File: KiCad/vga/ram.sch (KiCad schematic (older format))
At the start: 4 parts, among them U2 61256-15, U3 61256-15, U4 61256-15, U5 61256-15

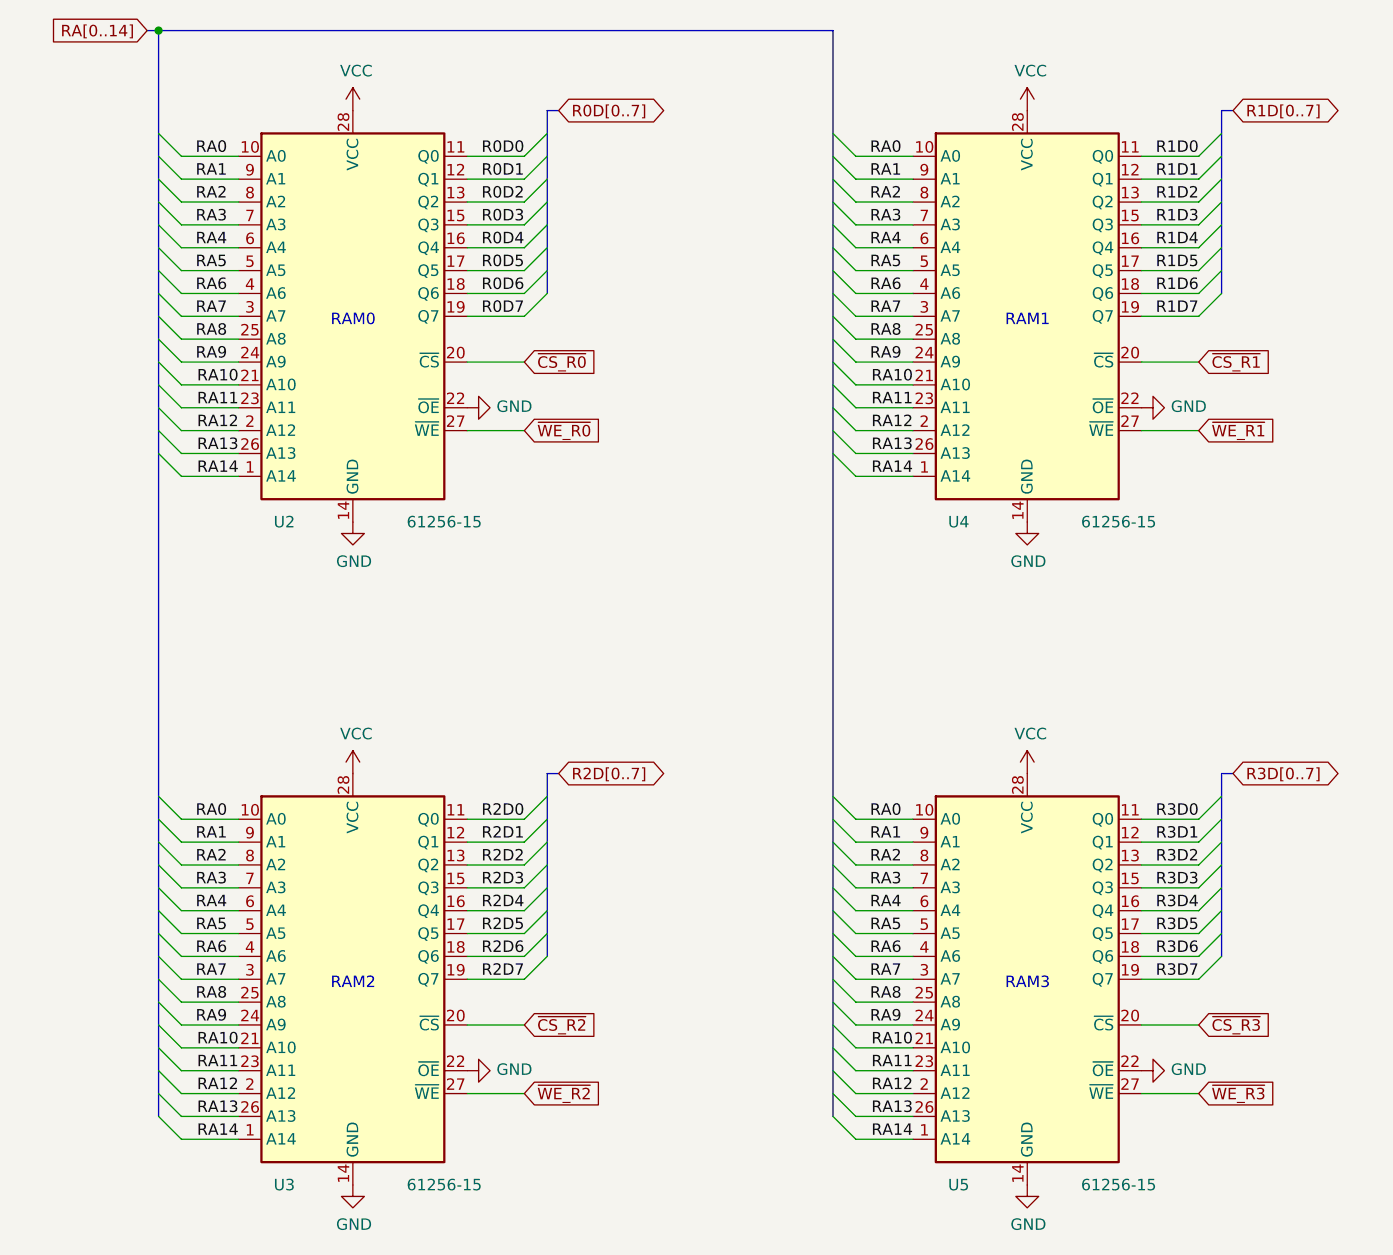
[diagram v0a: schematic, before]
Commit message: Updated graphics adapter
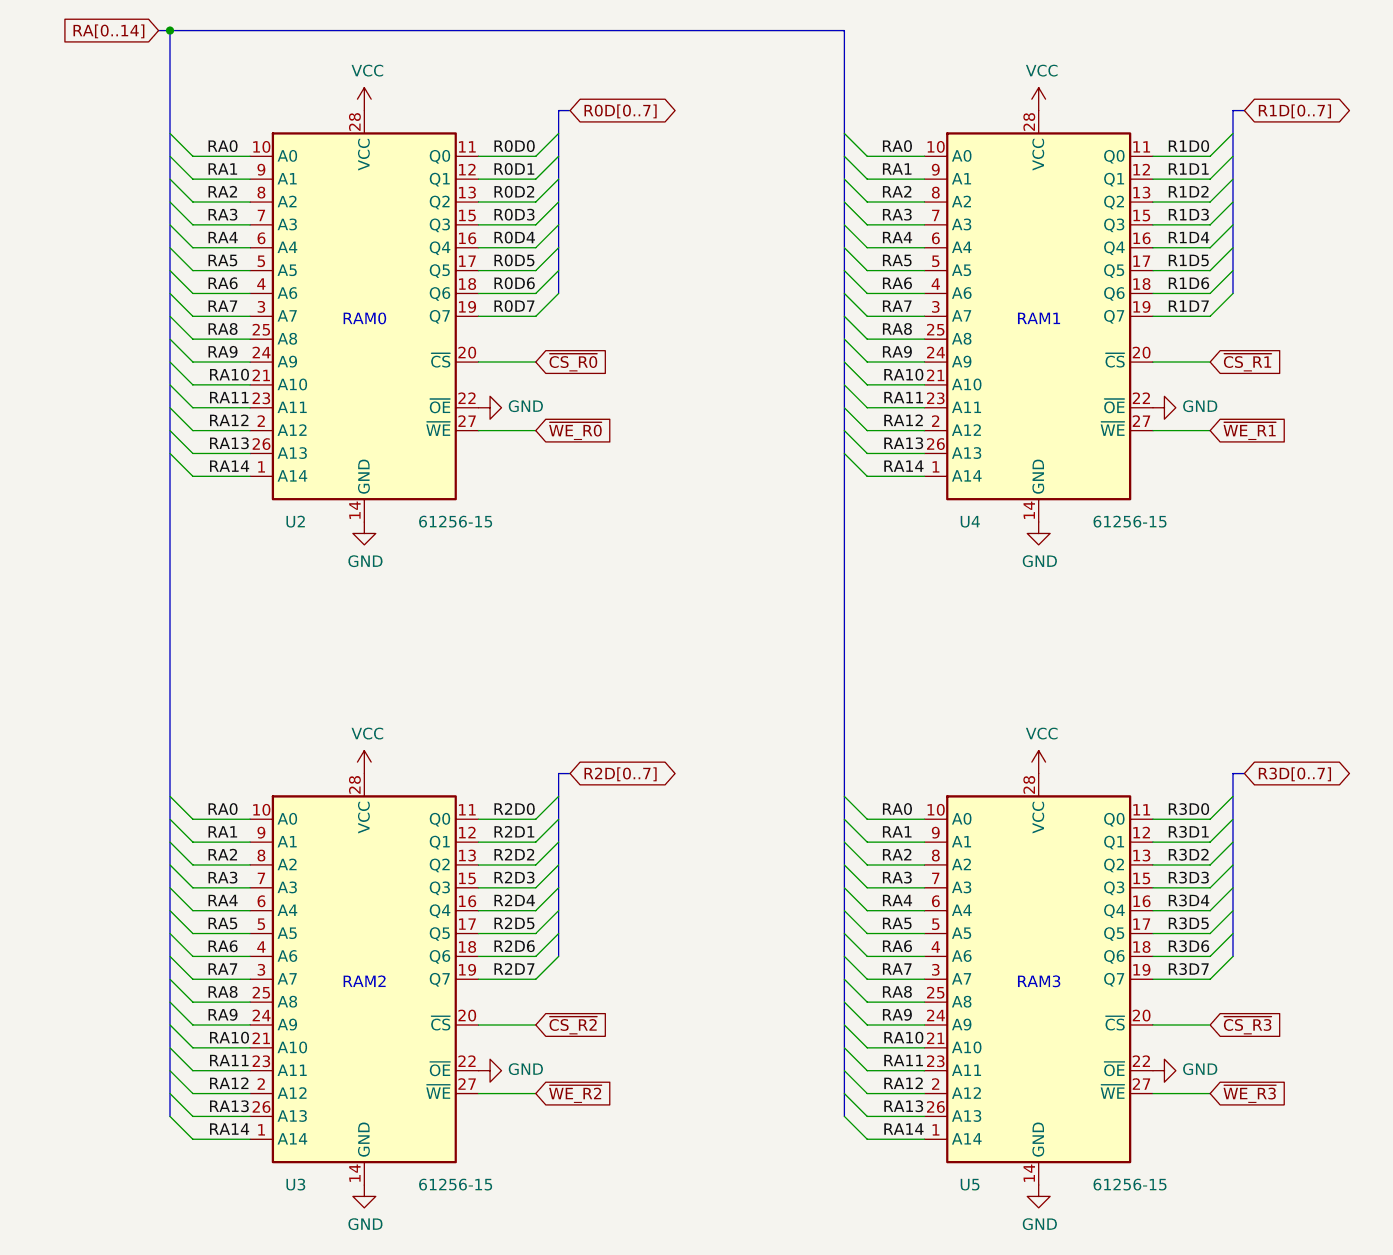
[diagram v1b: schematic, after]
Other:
- moved on the sheet: U2, U3, U4, U5

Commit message: Replaced MAX7000 CPLD with MAX II in graphics adapter. PCB redesign with smaller size.
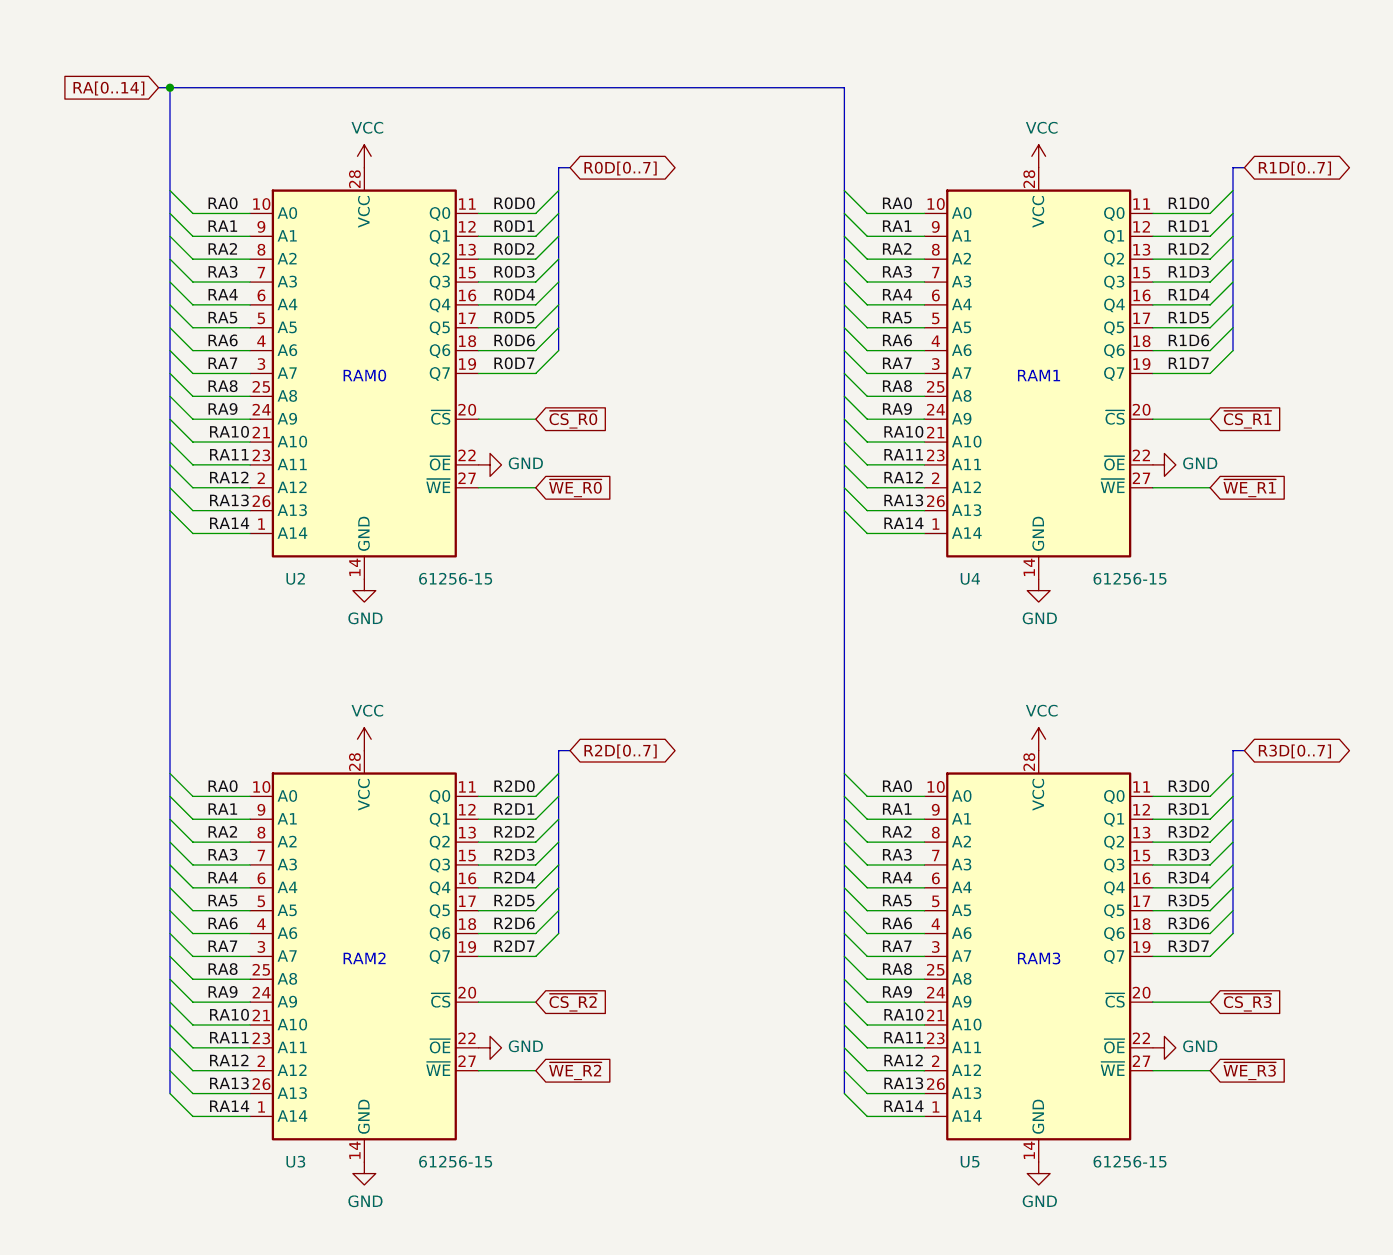
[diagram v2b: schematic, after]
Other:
- moved on the sheet: U2, U3, U4, U5
